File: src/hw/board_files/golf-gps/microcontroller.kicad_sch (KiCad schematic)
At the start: 14 parts, among them SW2 RESET, U4 STM32L432KCU6, Y1 32.768kHz

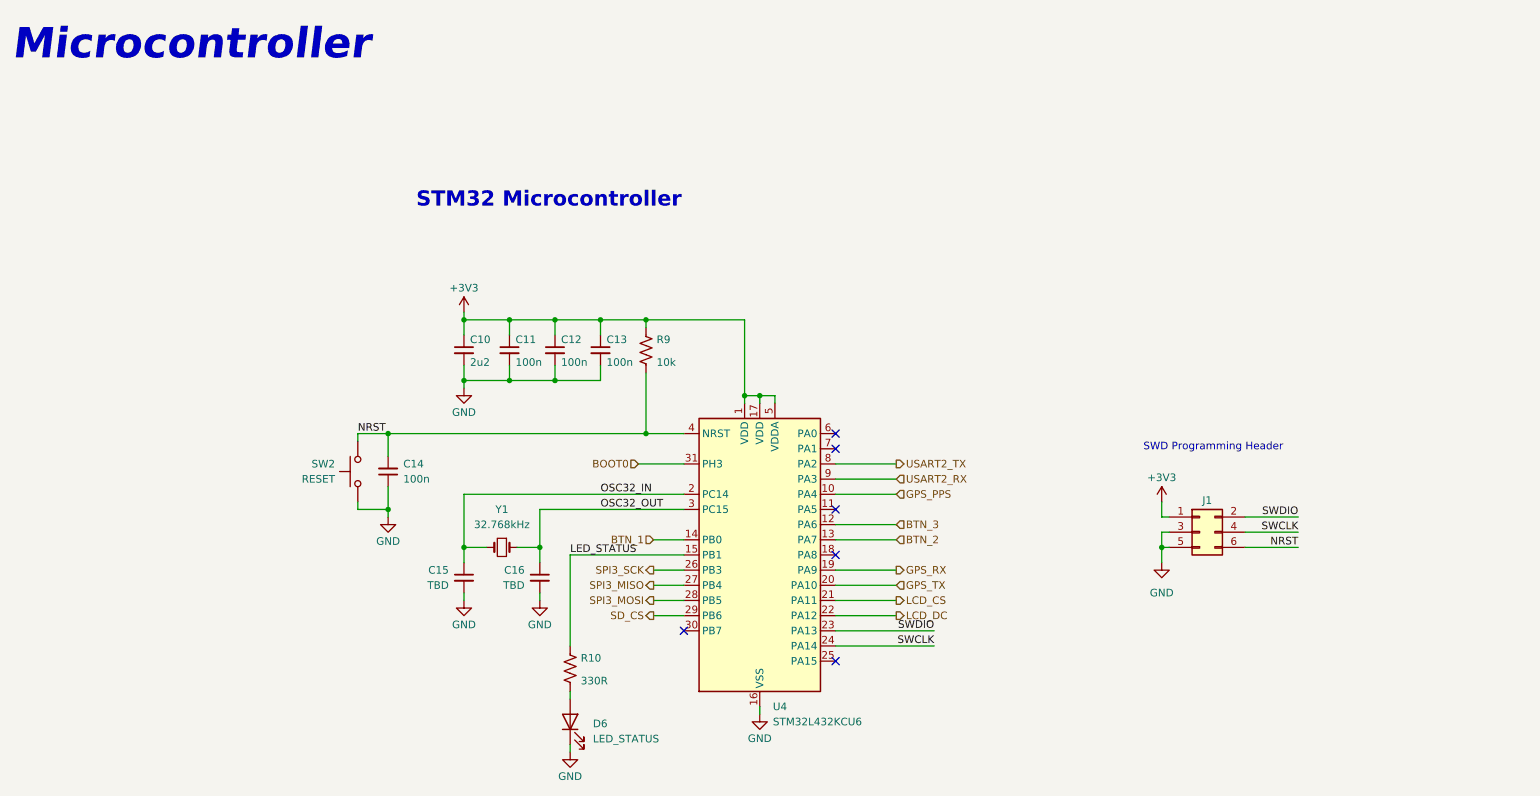
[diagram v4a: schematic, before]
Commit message: Removed USB to UART bridge, added VDDA decoupling, adjusted MCU pinout and updated spreadsheet
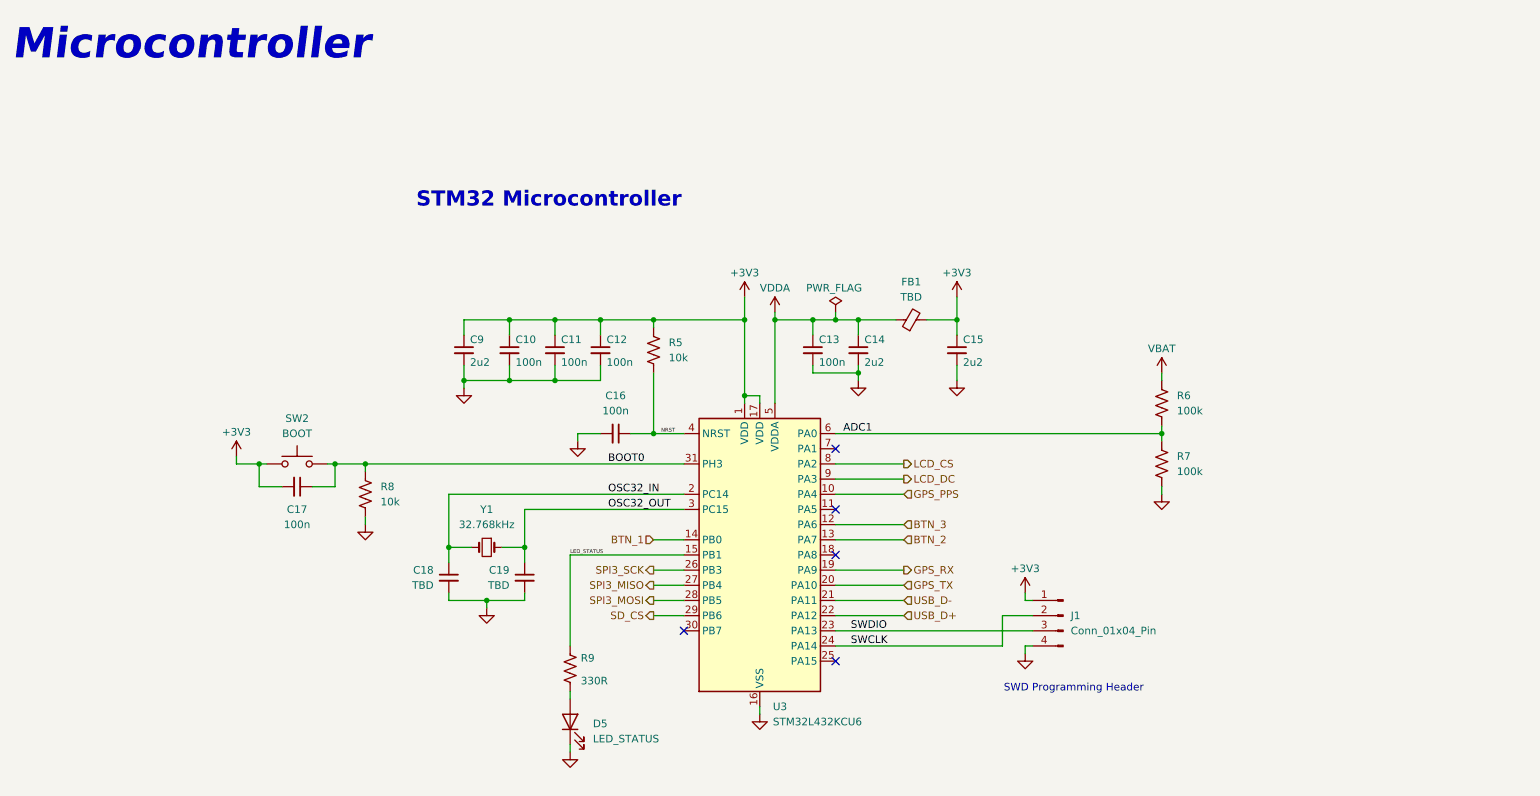
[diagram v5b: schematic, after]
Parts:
- removed J1: ~, Connector_PinHeader_2.54mm:PinHeader_2x03_P2.54mm_Vertical_SMD, symbol Connector_Generic:Conn_02x03_Odd_Even
- added C13, C17: 100n, Capacitor_SMD:C_0603_1608Metric, symbol Device:C_Small
- added C14, C15: 2u2, Capacitor_SMD:C_0603_1608Metric, symbol Device:C_Small
- added FB1: TBD, Inductor_SMD:L_0603_1608Metric, symbol Device:FerriteBead_Small
- added J1: Conn_01x04_Pin, Connector_PinHeader_2.54mm:PinHeader_1x04_P2.54mm_Horizontal, symbol Connector:Conn_01x04_Pin
- added R6, R7: 100k, Resistor_SMD:R_0603_1608Metric, symbol Device:R_US
- added R8: 10k, Resistor_SMD:R_0603_1608Metric, symbol Device:R_US
- SW2: value RESET -> BOOT
- renumbered C11 to C10, C12 to C11, C13 to C12, C14 to C16, C15 to C18, C16 to C19, C10 to C9, D6 to D5, R9 to R5, R10 to R9, U4 to U3
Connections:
- net USART2_RX is gone; now on net LCD_DC: U3.9 (PA3)
- net USART2_TX is gone; now on net LCD_CS: U3.8 (PA2)
- net +3V3: now also R5.2, SW2.2, C15.1, C17.2, FB1.2, J1.1 (Pin_1); no longer R5.1, U3.5 (VDDA)
- net BOOT0: now also SW2.1, C17.1, R8.1
- net GND: now also C16.2, C13.2, C14.2, C15.2, J1.4 (Pin_4), R7.1, R8.2; no longer C16.1, SW2.2
- net LCD_CS: no longer U3.21 (PA11)
- net LCD_DC: no longer U3.22 (PA12)
- net NRST: now also C16.1, R5.1; no longer C16.2, R5.2, SW2.1
- net SWCLK: now also J1.2 (Pin_2)
- net SWDIO: now also J1.3 (Pin_3)
- net ADC1: now reaches U3.6 (PA0)
- net ADC1: now also R6.1, R7.2
- new net USB_D+: U3.22 (PA12)
- new net USB_D-: U3.21 (PA11)
- new net VBAT: R6.2
- new net VDDA: C13.1, C14.1, FB1.1, U3.5 (VDDA)
- no-connect marks 6 -> 5
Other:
- moved on the sheet: C16, C18, C19, R5, Y1
